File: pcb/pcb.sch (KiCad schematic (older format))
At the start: 3 parts, among them J1 Raspberry Pi B+ 40-pin header, J2 12V Supply, J3 5V Supply

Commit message: Updating PCB
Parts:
- removed J1: Raspberry Pi B+ 40-pin header, Pin_Headers:Pin_Header_Straight_2x20, symbol Raspberry_Pi_2_3
- removed J2: 12V Supply, symbol CONN_01X02
- removed J3: 5V Supply, symbol CONN_01X02
- added A1: Arduino_Nano_v3.x, Module:Arduino_Nano, symbol MCU_Module:Arduino_Nano_v3.x
- added C1, C2: 22pF, Capacitor_THT:C_Disc_D5.0mm_W2.5mm_P2.50mm, symbol Device:C_Small
- added H1, H2, H3, H4: MountingHole, MountingHole:MountingHole_4.3mm_M4, symbol Mechanical:MountingHole
- added J1, J2: Barrel_Jack, Connector_BarrelJack:BarrelJack_CUI_PJ-102AH_Horizontal, symbol Connector:Barrel_Jack_Switch
- added J3: Screw_Terminal_01x03, TerminalBlock_TE-Connectivity:TerminalBlock_TE_282834-3_1x03_P2.54mm_Horizontal, symbol Connector:Screw_Terminal_01x03
- added J4: Screw_Terminal_01x02, TerminalBlock_TE-Connectivity:TerminalBlock_TE_282834-2_1x02_P2.54mm_Horizontal, symbol Connector:Screw_Terminal_01x02
- added J5: Conn_02x05_Odd_Even, Connector_IDC:IDC-Header_2x05_P2.54mm_Vertical, symbol Connector_Generic:Conn_02x05_Odd_Even
- added J6: Conn_01x06_Male, Connector_PinHeader_2.54mm:PinHeader_1x06_P2.54mm_Horizontal, symbol Connector:Conn_01x06_Male
- added R65, R66: 470, Resistor_THT:R_Axial_DIN0207_L6.3mm_D2.5mm_P7.62mm_Horizontal, symbol Device:R
- added SW1: SW_SPDT, digikey-footprints:Switch_Slide_11.6x4mm_EG1218, symbol Switch:SW_SPDT
- added U1: CPC5001G, Package_DIP:DIP-8_W7.62mm, symbol pcb:CPC5001G
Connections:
- net labels added: +9V, GNDcomm, INTA1, INTA2, INTB1, INTB2, PRG_MODE, RX, RXout, TX, TXout, Vcomm, ~RESET_IN1, ~RESET_IN2, ~RESET_OUT1, ~RESET_OUT2
- net labels removed: +3V3, RESET
- wire segments 55 -> 106
- no-connect marks 33 -> 20
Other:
- note added: "0x20"
- note added: "0x21"
- note added: "0x22"
- note added: "0x23"
- note added: "Arduino"
- note added: "Mounting\nholes"
- note added: "Power"
- note added: "Serial communication"
- note removed: "12V supply\nfor input"
- note removed: "5V supply\nfor logic"

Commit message: update
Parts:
- H1, H2, H3, H4: footprint MountingHole:MountingHole_4.3mm_M4 -> MountingHole:MountingHole_3.2mm_M3
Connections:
- net ~RESET_IN2: now also A1.12 (D9); no longer A1.10 (D7)
- net ~RESET_OUT2: now also A1.10 (D7); no longer A1.12 (D9)
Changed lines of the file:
@@
 F 0 "H1" H 5000 1296 50  0000 L CNN
 F 1 "MountingHole" H 5000 1205 50  0000 L CNN
-F 2 "MountingHole:MountingHole_4.3mm_M4" H 4900 1250 50  0001 C CNN
+F 2 "MountingHole:MountingHole_3.2mm_M3" H 4900 1250 50  0001 C CNN
 F 3 "~" H 4900 1250 50  0001 C CNN
 	1    4900 1250
@@
 F 0 "H2" H 5000 1546 50  0000 L CNN
 F 1 "MountingHole" H 5000 1455 50  0000 L CNN
-F 2 "MountingHole:MountingHole_4.3mm_M4" H 4900 1500 50  0001 C CNN
+F 2 "MountingHole:MountingHole_3.2mm_M3" H 4900 1500 50  0001 C CNN
 F 3 "~" H 4900 1500 50  0001 C CNN
 	1    4900 1500
@@
 F 0 "H3" H 5000 1796 50  0000 L CNN
 F 1 "MountingHole" H 5000 1705 50  0000 L CNN
-F 2 "MountingHole:MountingHole_4.3mm_M4" H 4900 1750 50  0001 C CNN
+F 2 "MountingHole:MountingHole_3.2mm_M3" H 4900 1750 50  0001 C CNN
 F 3 "~" H 4900 1750 50  0001 C CNN
 	1    4900 1750
@@
 F 0 "H4" H 5000 2046 50  0000 L CNN
 F 1 "MountingHole" H 5000 1955 50  0000 L CNN
-F 2 "MountingHole:MountingHole_4.3mm_M4" H 4900 2000 50  0001 C CNN
+F 2 "MountingHole:MountingHole_3.2mm_M3" H 4900 2000 50  0001 C CNN
 F 3 "~" H 4900 2000 50  0001 C CNN
 	1    4900 2000
@@
 Text Label 950  3850 0    50   ~ 0
 ~RESET_IN1
-Text Label 950  3950 0    50   ~ 0
+Text Label 950  4150 0    50   ~ 0
 ~RESET_IN2
 Text Label 950  4050 0    50   ~ 0
 ~RESET_OUT1
-Text Label 950  4150 0    50   ~ 0
+Text Label 950  3950 0    50   ~ 0
 ~RESET_OUT2
 Wire Wire Line

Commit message: Update
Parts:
- C1, C2: value 22pF -> 0.1uF
- H1, H2, H3, H4: footprint MountingHole:MountingHole_3.2mm_M3 -> MountingHole:MountingHole_4.3mm_M4
- R65, R66: value 470 -> 1k
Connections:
- net +5V: now also C2.1; no longer C2.2
- net GND: now also C2.2; no longer C2.1
- net GNDcomm: now also C1.1; no longer C1.2
- net Vcomm: now also C1.2; no longer C1.1
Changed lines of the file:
@@
 F 0 "H1" H 5000 1296 50  0000 L CNN
 F 1 "MountingHole" H 5000 1205 50  0000 L CNN
-F 2 "MountingHole:MountingHole_3.2mm_M3" H 4900 1250 50  0001 C CNN
+F 2 "MountingHole:MountingHole_4.3mm_M4" H 4900 1250 50  0001 C CNN
 F 3 "~" H 4900 1250 50  0001 C CNN
 	1    4900 1250
@@
 F 0 "H2" H 5000 1546 50  0000 L CNN
 F 1 "MountingHole" H 5000 1455 50  0000 L CNN
-F 2 "MountingHole:MountingHole_3.2mm_M3" H 4900 1500 50  0001 C CNN
+F 2 "MountingHole:MountingHole_4.3mm_M4" H 4900 1500 50  0001 C CNN
 F 3 "~" H 4900 1500 50  0001 C CNN
 	1    4900 1500
@@
 F 0 "H3" H 5000 1796 50  0000 L CNN
 F 1 "MountingHole" H 5000 1705 50  0000 L CNN
-F 2 "MountingHole:MountingHole_3.2mm_M3" H 4900 1750 50  0001 C CNN
+F 2 "MountingHole:MountingHole_4.3mm_M4" H 4900 1750 50  0001 C CNN
 F 3 "~" H 4900 1750 50  0001 C CNN
 	1    4900 1750
@@
 F 0 "H4" H 5000 2046 50  0000 L CNN
 F 1 "MountingHole" H 5000 1955 50  0000 L CNN
-F 2 "MountingHole:MountingHole_3.2mm_M3" H 4900 2000 50  0001 C CNN
+F 2 "MountingHole:MountingHole_4.3mm_M4" H 4900 2000 50  0001 C CNN
 F 3 "~" H 4900 2000 50  0001 C CNN
 	1    4900 2000
@@
 	1    0    0    -1
 $EndComp
-$Comp
-L Device:C_Small C1
-U 1 1 5C2A0087
-P 7650 2450
-F 0 "C1" H 7558 2404 50  0000 R CNN
-F 1 "22pF" H 7558 2495 50  0000 R CNN
-F 2 "Capacitor_THT:C_Disc_D5.0mm_W2.5mm_P2.50mm" H 7650 2450 50  0001 C CNN
-F 3 "~" H 7650 2450 50  0001 C CNN
-	1    7650 2450
-	-1   0    0    1
-$EndComp
 Wire Wire Line
 	8000 2550 7650 2550
 Wire Wire Line
-	8000 2350 7650 2350
-$Comp
-L Device:C_Small C2
-U 1 1 5C2A4A63
-P 9300 2350
-F 0 "C2" H 9208 2304 50  0000 R CNN
-F 1 "22pF" H 9208 2395 50  0000 R CNN
-F 2 "Capacitor_THT:C_Disc_D5.0mm_W2.5mm_P2.50mm" H 9300 2350 50  0001 C CNN
-F 3 "~" H 9300 2350 50  0001 C CNN
-	1    9300 2350
-	-1   0    0    1
-$EndComp
-Wire Wire Line
 	9300 2250 9150 2250
 Wire Wire Line
-	8800 2450 9300 2450
+	8800 2450 9150 2450
 Text Label 7200 2350 0    50   ~ 0
 GNDcomm
@@
 Vcomm
 Connection ~ 7650 2550
-Connection ~ 7650 2350
-Wire Wire Line
-	7200 2350 7650 2350
 Wire Wire Line
 	7200 2550 7650 2550
 Wire Wire Line
 	9300 2250 9300 2150
-Connection ~ 9300 2250
 $Comp
 L power:+5V #PWR0103
@@
 Wire Wire Line
 	9300 2450 9300 2550
-Connection ~ 9300 2450
 Wire Wire Line
 	8800 2350 8850 2350
@@
 P 8850 2000
 F 0 "R66" H 8920 2046 50  0000 L CNN
-F 1 "470" H 8920 1955 50  0000 L CNN
+F 1 "1k" H 8920 1955 50  0000 L CNN
 F 2 "Resistor_THT:R_Axial_DIN0207_L6.3mm_D2.5mm_P7.62mm_Horizontal" V 8780 2000 50  0001 C CNN
 F 3 "~" H 8850 2000 50  0001 C CNN
@@
 P 7650 2700
 F 0 "R65" H 7720 2746 50  0000 L CNN
-F 1 "470" H 7720 2655 50  0000 L CNN
+F 1 "1k" H 7720 2655 50  0000 L CNN
 F 2 "Resistor_THT:R_Axial_DIN0207_L6.3mm_D2.5mm_P7.62mm_Horizontal" V 7580 2700 50  0001 C CNN
 F 3 "~" H 7650 2700 50  0001 C CNN
@@
 Text Label 7200 2850 0    50   ~ 0
 TXout
+Wire Wire Line
+	7200 2350 7650 2350
+$Comp
+L Device:C_Small C1
+U 1 1 5C2EE7BD
+P 7650 2450
+F 0 "C1" H 7742 2496 50  0000 L CNN
+F 1 "0.1uF" H 7742 2405 50  0000 L CNN
+F 2 "Capacitor_THT:C_Disc_D5.0mm_W2.5mm_P2.50mm" H 7650 2450 50  0001 C CNN
+F 3 "~" H 7650 2450 50  0001 C CNN
+	1    7650 2450
+	1    0    0    -1
+$EndComp
+Connection ~ 7650 2350
+Wire Wire Line
+	7650 2350 8000 2350
+$Comp
+L Device:C_Small C2
+U 1 1 5C2EE82F
+P 9150 2350
+F 0 "C2" H 9242 2396 50  0000 L CNN
+F 1 "0.1uF" H 9242 2305 50  0000 L CNN
+F 2 "Capacitor_THT:C_Disc_D5.0mm_W2.5mm_P2.50mm" H 9150 2350 50  0001 C CNN
+F 3 "~" H 9150 2350 50  0001 C CNN
+	1    9150 2350
+	1    0    0    -1
+$EndComp
+Connection ~ 9150 2450
+Wire Wire Line
+	9150 2450 9300 2450
 $EndSCHEMATC

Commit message: latest
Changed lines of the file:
@@
 Power
 $Sheet
-S 4850 3550 950  700
+S 1400 5650 950  700
 U 5C211542
 F0 "Input 1" 50
 F1 "input.sch" 50
-F2 "A0" I L 4850 3650 50
-F3 "A1" I L 4850 3750 50
-F4 "A2" I L 4850 3850 50
-F5 "INTA" I L 4850 3950 50
-F6 "INTB" I L 4850 4050 50
-F7 "~RESET" I L 4850 4150 50
+F2 "A0" I L 1400 5750 50
+F3 "A1" I L 1400 5850 50
+F4 "A2" I L 1400 5950 50
+F5 "INTA" I L 1400 6050 50
+F6 "INTB" I L 1400 6150 50
+F7 "~RESET" I L 1400 6250 50
 $EndSheet
 $Sheet
-S 4850 4500 950  700
+S 1400 6600 950  700
 U 5C211551
 F0 "Input 2" 50
 F1 "input.sch" 50
-F2 "A0" I L 4850 4600 50
-F3 "A1" I L 4850 4700 50
-F4 "A2" I L 4850 4800 50
-F5 "INTA" I L 4850 4900 50
-F6 "INTB" I L 4850 5000 50
-F7 "~RESET" I L 4850 5100 50
+F2 "A0" I L 1400 6700 50
+F3 "A1" I L 1400 6800 50
+F4 "A2" I L 1400 6900 50
+F5 "INTA" I L 1400 7000 50
+F6 "INTB" I L 1400 7100 50
+F7 "~RESET" I L 1400 7200 50
 $EndSheet
 $Comp
 L power:GND #PWR019
 U 1 1 5C24134C
-P 4700 5200
-F 0 "#PWR019" H 4700 4950 50  0001 C CNN
-F 1 "GND" H 4705 5027 50  0000 C CNN
-F 2 "" H 4700 5200 50  0001 C CNN
-F 3 "" H 4700 5200 50  0001 C CNN
-	1    4700 5200
+P 1250 7300
+F 0 "#PWR019" H 1250 7050 50  0001 C CNN
+F 1 "GND" H 1255 7127 50  0000 C CNN
+F 2 "" H 1250 7300 50  0001 C CNN
+F 3 "" H 1250 7300 50  0001 C CNN
+	1    1250 7300
 	1    0    0    -1
 $EndComp
@@
 L power:+5V #PWR018
 U 1 1 5C2413B9
-P 4600 3600
-F 0 "#PWR018" H 4600 3450 50  0001 C CNN
-F 1 "+5V" H 4615 3773 50  0000 C CNN
-F 2 "" H 4600 3600 50  0001 C CNN
-F 3 "" H 4600 3600 50  0001 C CNN
-	1    4600 3600
-	1    0    0    -1
-$EndComp
-Wire Wire Line
-	4850 3650 4700 3650
-Wire Wire Line
-	4700 3650 4700 3750
-Wire Wire Line
-	4850 3750 4700 3750
-Connection ~ 4700 3750
-Wire Wire Line
-	4700 3750 4700 3850
-Wire Wire Line
-	4850 3850 4700 3850
-Wire Wire Line
-	4850 4700 4700 4700
-Wire Wire Line
-	4700 4700 4700 4800
-Wire Wire Line
-	4850 4800 4700 4800
-Text Notes 4850 3450 0    50   ~ 0
+P 1150 5700
+F 0 "#PWR018" H 1150 5550 50  0001 C CNN
+F 1 "+5V" H 1165 5873 50  0000 C CNN
+F 2 "" H 1150 5700 50  0001 C CNN
+F 3 "" H 1150 5700 50  0001 C CNN
+	1    1150 5700
+	1    0    0    -1
+$EndComp
+Wire Wire Line
+	1400 5750 1250 5750
+Wire Wire Line
+	1250 5750 1250 5850
+Wire Wire Line
+	1400 5850 1250 5850
+Connection ~ 1250 5850
+Wire Wire Line
+	1250 5850 1250 5950
+Wire Wire Line
+	1400 5950 1250 5950
+Wire Wire Line
+	1400 6800 1250 6800
+Wire Wire Line
+	1250 6800 1250 6900
+Wire Wire Line
+	1400 6900 1250 6900
+Text Notes 1400 5550 0    50   ~ 0
 0x20
-Text Notes 4850 4400 0    50   ~ 0
+Text Notes 1400 6500 0    50   ~ 0
 0x21
 $Sheet
-S 6050 3750 950  500
+S 2600 5850 950  500
 U 5C242719
 F0 "Output 1" 50
 F1 "output.sch" 50
-F2 "A0" I R 7000 3850 50
-F3 "A1" I R 7000 3950 50
-F4 "A2" I R 7000 4050 50
-F5 "~RESET" I R 7000 4150 50
+F2 "A0" I R 3550 5950 50
+F3 "A1" I R 3550 6050 50
+F4 "A2" I R 3550 6150 50
+F5 "~RESET" I R 3550 6250 50
 $EndSheet
 $Sheet
-S 6050 4500 950  500
+S 2600 6600 950  500
 U 5C24272E
 F0 "Output 2" 50
 F1 "output.sch" 50
-F2 "A0" I R 7000 4600 50
-F3 "A1" I R 7000 4700 50
-F4 "A2" I R 7000 4800 50
-F5 "~RESET" I R 7000 4900 50
+F2 "A0" I R 3550 6700 50
+F3 "A1" I R 3550 6800 50
+F4 "A2" I R 3550 6900 50
+F5 "~RESET" I R 3550 7000 50
 $EndSheet
 $Comp
 L power:GND #PWR020
 U 1 1 5C2430F8
-P 7200 5150
-F 0 "#PWR020" H 7200 4900 50  0001 C CNN
-F 1 "GND" H 7205 4977 50  0000 C CNN
-F 2 "" H 7200 5150 50  0001 C CNN
-F 3 "" H 7200 5150 50  0001 C CNN
-	1    7200 5150
-	1    0    0    -1
-$EndComp
-Wire Wire Line
-	7000 4050 7200 4050
-Wire Wire Line
-	7200 4050 7200 4800
-Wire Wire Line
-	7000 4800 7200 4800
-Connection ~ 7200 4800
-Wire Wire Line
-	7200 4800 7200 5150
-Wire Wire Line
-	7000 3850 7200 3850
-Wire Wire Line
-	7200 3850 7200 4050
-Connection ~ 7200 4050
+P 3750 7250
+F 0 "#PWR020" H 3750 7000 50  0001 C CNN
+F 1 "GND" H 3755 7077 50  0000 C CNN
+F 2 "" H 3750 7250 50  0001 C CNN
+F 3 "" H 3750 7250 50  0001 C CNN
+	1    3750 7250
+	1    0    0    -1
+$EndComp
+Wire Wire Line
+	3550 6150 3750 6150
+Wire Wire Line
+	3750 6150 3750 6900
+Wire Wire Line
+	3550 6900 3750 6900
+Connection ~ 3750 6900
+Wire Wire Line
+	3750 6900 3750 7250
+Wire Wire Line
+	3550 5950 3750 5950
+Wire Wire Line
+	3750 5950 3750 6150
+Connection ~ 3750 6150
 $Comp
 L power:+5V #PWR021
 U 1 1 5C243E0C
-P 7400 3600
-F 0 "#PWR021" H 7400 3450 50  0001 C CNN
-F 1 "+5V" H 7415 3773 50  0000 C CNN
-F 2 "" H 7400 3600 50  0001 C CNN
-F 3 "" H 7400 3600 50  0001 C CNN
-	1    7400 3600
-	1    0    0    -1
-$EndComp
-Wire Wire Line
-	7400 3600 7400 3950
-Wire Wire Line
-	7400 3950 7000 3950
-Wire Wire Line
-	7400 3950 7400 4600
-Wire Wire Line
-	7400 4600 7000 4600
-Connection ~ 7400 3950
-Wire Wire Line
-	7000 4700 7400 4700
-Wire Wire Line
-	7400 4700 7400 4600
-Connection ~ 7400 4600
+P 3950 5700
+F 0 "#PWR021" H 3950 5550 50  0001 C CNN
+F 1 "+5V" H 3965 5873 50  0000 C CNN
+F 2 "" H 3950 5700 50  0001 C CNN
+F 3 "" H 3950 5700 50  0001 C CNN
+	1    3950 5700
+	1    0    0    -1
+$EndComp
+Wire Wire Line
+	3950 5700 3950 6050
+Wire Wire Line
+	3950 6050 3550 6050
+Wire Wire Line
+	3950 6050 3950 6700
+Wire Wire Line
+	3950 6700 3550 6700
+Connection ~ 3950 6050
+Wire Wire Line
+	3550 6800 3950 6800
+Wire Wire Line
+	3950 6800 3950 6700
+Connection ~ 3950 6700
 $Comp
 L Connector:Screw_Terminal_01x02 J4
@@
 $EndComp
 Wire Wire Line
-	4600 3600 4600 4600
-Wire Wire Line
-	4250 3950 4850 3950
-Wire Wire Line
-	4250 4050 4850 4050
-Wire Wire Line
-	4250 5000 4850 5000
-Text Label 4250 3950 0    50   ~ 0
+	1150 5700 1150 6700
+Wire Wire Line
+	800  6050 1400 6050
+Wire Wire Line
+	800  6150 1400 6150
+Wire Wire Line
+	800  7100 1400 7100
+Text Label 800  6050 0    50   ~ 0
 INTA1
-Text Label 4250 4050 0    50   ~ 0
+Text Label 800  6150 0    50   ~ 0
 INTB1
-Text Label 4250 4900 0    50   ~ 0
+Text Label 800  7000 0    50   ~ 0
 INTA2
-Text Label 4250 5000 0    50   ~ 0
+Text Label 800  7100 0    50   ~ 0
 INTB2
 Text Label 950  3450 0    50   ~ 0
@@
 INTB2
 Wire Wire Line
-	4250 4150 4850 4150
-Text Label 4250 4150 0    50   ~ 0
+	800  6250 1400 6250
+Text Label 800  6250 0    50   ~ 0
 ~RESET_IN1
 Wire Wire Line
-	4250 4900 4850 4900
-Wire Wire Line
-	4700 5200 4700 4800
-Connection ~ 4700 4800
-Wire Wire Line
-	4600 4600 4850 4600
-Wire Wire Line
-	4700 3850 4700 4700
-Connection ~ 4700 3850
-Connection ~ 4700 4700
-Wire Wire Line
-	4850 5100 4250 5100
-Text Label 4250 5100 0    50   ~ 0
+	800  7000 1400 7000
+Wire Wire Line
+	1250 7300 1250 6900
+Connection ~ 1250 6900
+Wire Wire Line
+	1150 6700 1400 6700
+Wire Wire Line
+	1250 5950 1250 6800
+Connection ~ 1250 5950
+Connection ~ 1250 6800
+Wire Wire Line
+	1400 7200 800  7200
+Text Label 800  7200 0    50   ~ 0
 ~RESET_IN2
 Wire Wire Line
-	7000 4150 7700 4150
-Wire Wire Line
-	7000 4900 7700 4900
-Text Label 7700 4150 0    50   ~ 0
+	3550 6250 4250 6250
+Wire Wire Line
+	3550 7000 4250 7000
+Text Label 4250 6250 0    50   ~ 0
 ~RESET_OUT1
-Text Label 7700 4900 0    50   ~ 0
+Text Label 4250 7000 0    50   ~ 0
 ~RESET_OUT2
 Text Label 950  3850 0    50   ~ 0
@@
 Text Label 8150 1550 0    50   ~ 0
 RXout
-Text Notes 6050 3650 0    50   ~ 0
+Text Notes 2600 5750 0    50   ~ 0
 0x22
-Text Notes 6050 4400 0    50   ~ 0
+Text Notes 2600 6500 0    50   ~ 0
 0x23
 Wire Notes Line
@@
 NoConn ~ 7800 1750
 Wire Notes Line
-	6050 850  6050 3100
-Wire Notes Line
-	10050 3100 10050 850
-Wire Notes Line
 	6050 850  10050 850
-Wire Notes Line
-	6050 3100 10050 3100
 $Comp
 L pcb:CPC5001G U1
@@
 Wire Wire Line
 	9150 2450 9300 2450
+Wire Notes Line
+	6050 850  6050 3100
+Wire Notes Line
+	6050 3100 10050 3100
+Wire Notes Line
+	10050 3100 10050 850
 $EndSCHEMATC

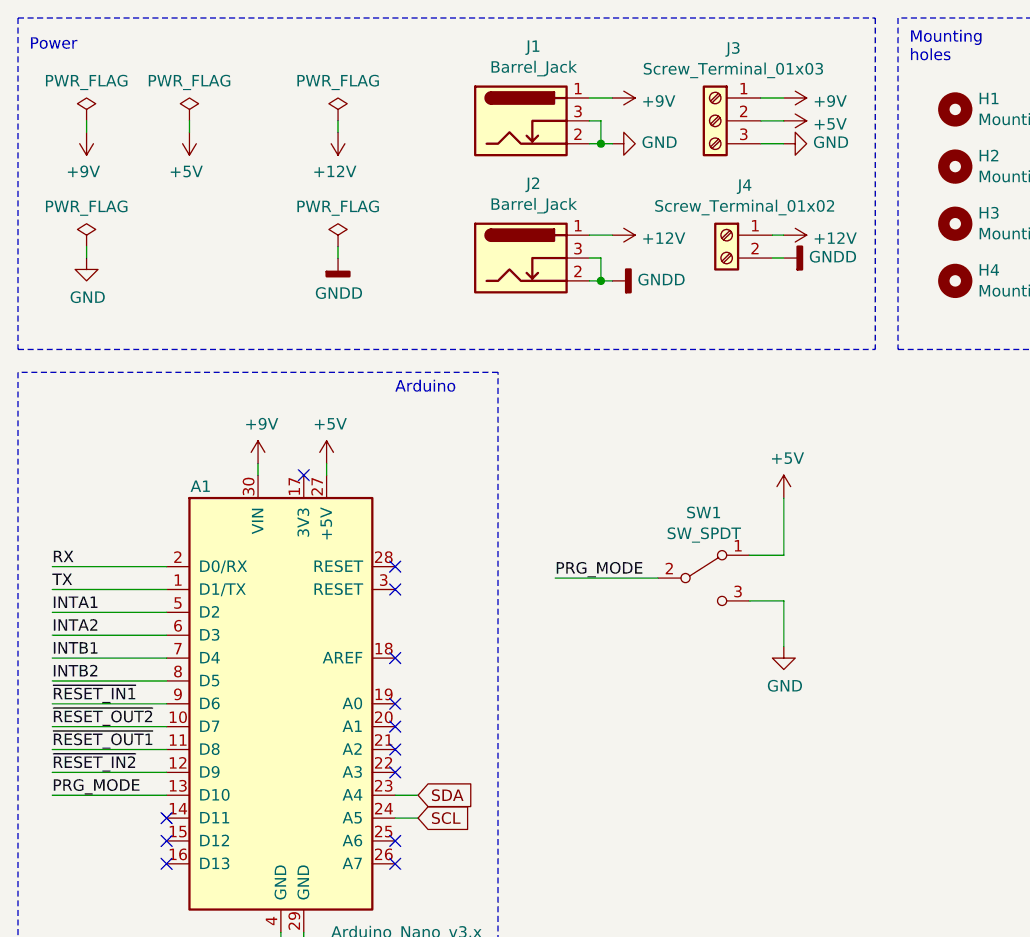
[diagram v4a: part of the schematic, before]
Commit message: 4 layer PCB
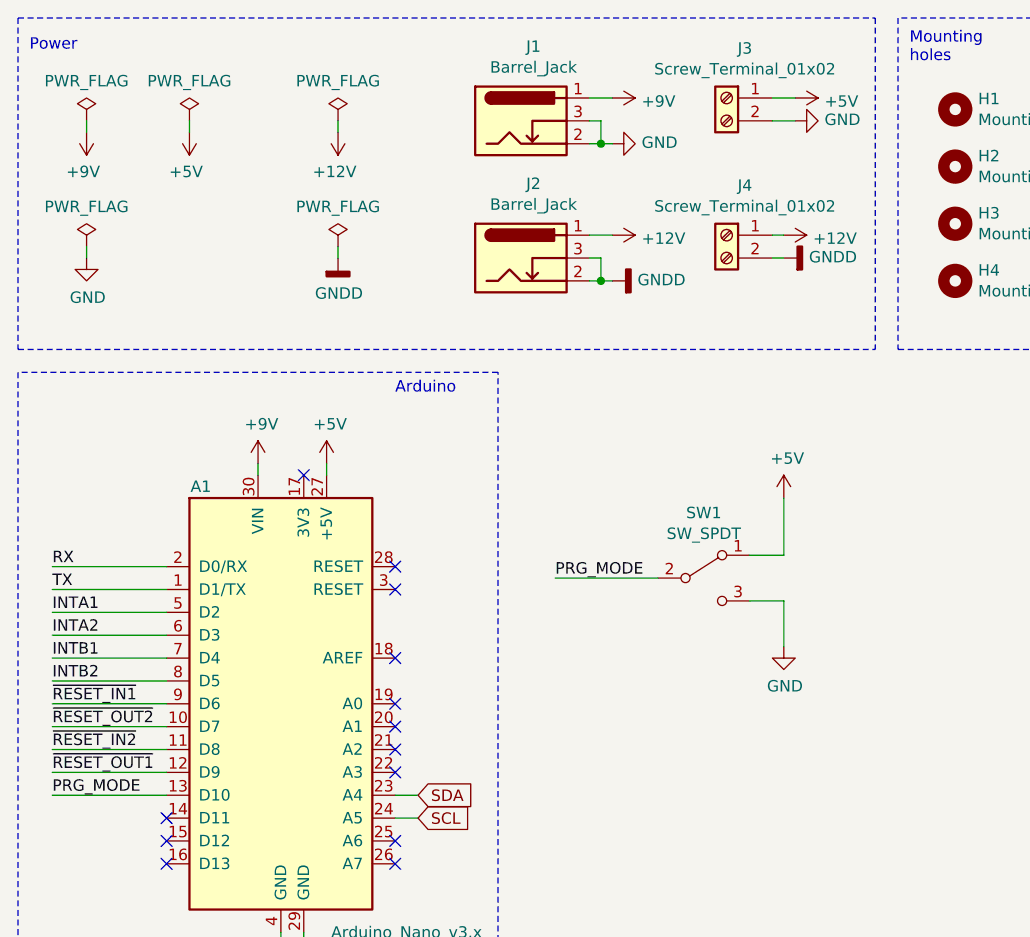
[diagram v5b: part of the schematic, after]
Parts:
- removed J3: Screw_Terminal_01x03, TerminalBlock_TE-Connectivity:TerminalBlock_TE_282834-3_1x03_P2.54mm_Horizontal, symbol Connector:Screw_Terminal_01x03
- added J3: Screw_Terminal_01x02, TerminalBlock_TE-Connectivity:TerminalBlock_TE_282834-2_1x02_P2.54mm_Horizontal, symbol Connector:Screw_Terminal_01x02
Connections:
- net +5V: now also J3.1 (Pin_1)
- net GND: now also J3.2 (Pin_2)
- net ~RESET_IN2: now also A1.11 (D8); no longer A1.12 (D9)
- net ~RESET_OUT1: now also A1.12 (D9); no longer A1.11 (D8)
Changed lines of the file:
@@
-$EndComp
-$Comp
-L Connector:Screw_Terminal_01x03 J3
-U 1 1 5C2CE585
-P 3850 1300
-F 0 "J3" H 3770 1617 50  0000 C CNN
-F 1 "Screw_Terminal_01x03" H 3770 1526 50  0000 C CNN
-F 2 "TerminalBlock_TE-Connectivity:TerminalBlock_TE_282834-3_1x03_P2.54mm_Horizontal" H 3850 1300 50  0001 C CNN
-F 3 "~" H 3850 1300 50  0001 C CNN
-	1    3850 1300
-	-1   0    0    -1
-$EndComp
-$Comp
-L power:+9V #PWR013
-U 1 1 5C2CE665
-P 4150 1200
-F 0 "#PWR013" H 4150 1050 50  0001 C CNN
-F 1 "+9V" V 4165 1328 50  0000 L CNN
-F 2 "" H 4150 1200 50  0001 C CNN
-F 3 "" H 4150 1200 50  0001 C CNN
-	1    4150 1200
-	0    1    1    0
 $EndComp
 $Comp
 L power:+5V #PWR014
 U 1 1 5C2CE6DE
-P 4150 1300
-F 0 "#PWR014" H 4150 1150 50  0001 C CNN
-F 1 "+5V" V 4165 1428 50  0000 L CNN
-F 2 "" H 4150 1300 50  0001 C CNN
-F 3 "" H 4150 1300 50  0001 C CNN
-	1    4150 1300
+P 4200 1200
+F 0 "#PWR014" H 4200 1050 50  0001 C CNN
+F 1 "+5V" V 4215 1328 50  0000 L CNN
+F 2 "" H 4200 1200 50  0001 C CNN
+F 3 "" H 4200 1200 50  0001 C CNN
+	1    4200 1200
 	0    1    1    0
 $EndComp
@@
 L power:GND #PWR015
 U 1 1 5C2CE757
-P 4150 1400
-F 0 "#PWR015" H 4150 1150 50  0001 C CNN
-F 1 "GND" V 4155 1272 50  0000 R CNN
-F 2 "" H 4150 1400 50  0001 C CNN
-F 3 "" H 4150 1400 50  0001 C CNN
-	1    4150 1400
+P 4200 1300
+F 0 "#PWR015" H 4200 1050 50  0001 C CNN
+F 1 "GND" V 4205 1172 50  0000 R CNN
+F 2 "" H 4200 1300 50  0001 C CNN
+F 3 "" H 4200 1300 50  0001 C CNN
+	1    4200 1300
 	0    -1   -1   0
 $EndComp
 Wire Wire Line
-	4050 1200 4150 1200
-Wire Wire Line
-	4150 1300 4050 1300
-Wire Wire Line
-	4050 1400 4150 1400
+	4200 1200 4100 1200
+Wire Wire Line
+	4100 1300 4200 1300
 Wire Notes Line
 	4550 850  4550 2300
@@
 Text Label 950  3850 0    50   ~ 0
 ~RESET_IN1
+Text Label 950  4050 0    50   ~ 0
+~RESET_IN2
 Text Label 950  4150 0    50   ~ 0
-~RESET_IN2
-Text Label 950  4050 0    50   ~ 0
 ~RESET_OUT1
 Text Label 950  3950 0    50   ~ 0
@@
 Wire Notes Line
 	10050 3100 10050 850
+$Comp
+L Connector:Screw_Terminal_01x02 J3
+U 1 1 5C3C8AB8
+P 3900 1200
+F 0 "J3" H 3820 1417 50  0000 C CNN
+F 1 "Screw_Terminal_01x02" H 3820 1326 50  0000 C CNN
+F 2 "TerminalBlock_TE-Connectivity:TerminalBlock_TE_282834-2_1x02_P2.54mm_Horizontal" H 3900 1200 50  0001 C CNN
+F 3 "~" H 3900 1200 50  0001 C CNN
+	1    3900 1200
+	-1   0    0    -1
+$EndComp
 $EndSCHEMATC
